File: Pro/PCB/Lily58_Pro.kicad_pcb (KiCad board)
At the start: 2 copper layers, 142.5 x 106.3 mm, 87 parts, among them J1 LED, J2 4PIN, J3 OLED, P1 i2c_pin, P2 i2c_pin, SW1 SW_PUSH, SW10 SW_PUSH, SW11 SW_PUSH, SW12 SW_PUSH, SW13 SW_PUSH, SW14 SW_PUSH, SW15 SW_PUSH, SW16 SW_PUSH, SW17 SW_PUSH, SW18 SW_PUSH, SW19 SW_PUSH, SW2 SW_PUSH, SW20 SW_PUSH, SW21 SW_PUSH, SW22 SW_PUSH, SW23 SW_PUSH, SW24 SW_PUSH, SW25 SW_PUSH, SW26 SW_PUSH, SW27 SW_PUSH, SW28 SW_PUSH, SW29 SW_PUSH, SW3 SW_PUSH, SW4 SW_PUSH, SW5 SW_PUSH, SW6 SW_PUSH, SW7 SW_PUSH, SW8 SW_PUSH, SW9 SW_PUSH, U1 ProMicro

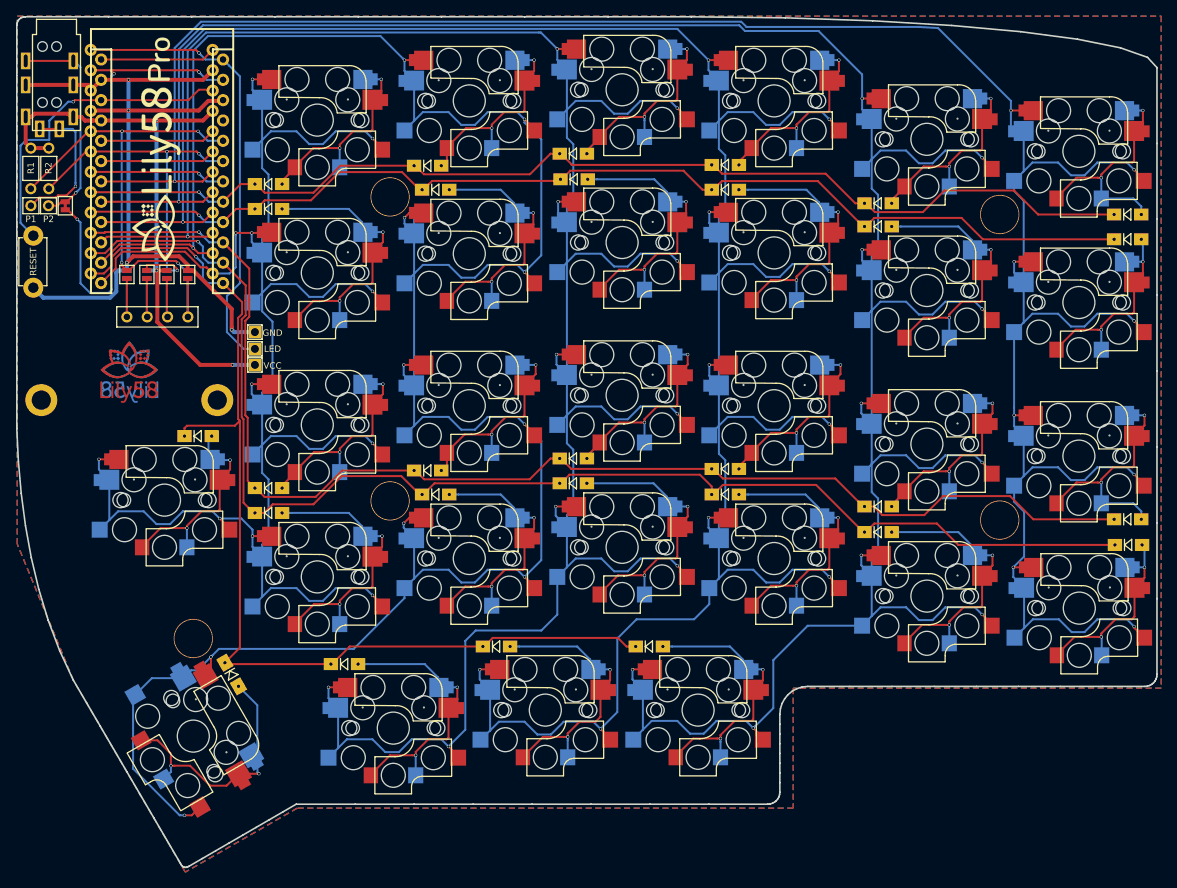
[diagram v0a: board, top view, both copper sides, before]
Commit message: Add footprints to Lily58 Pro library
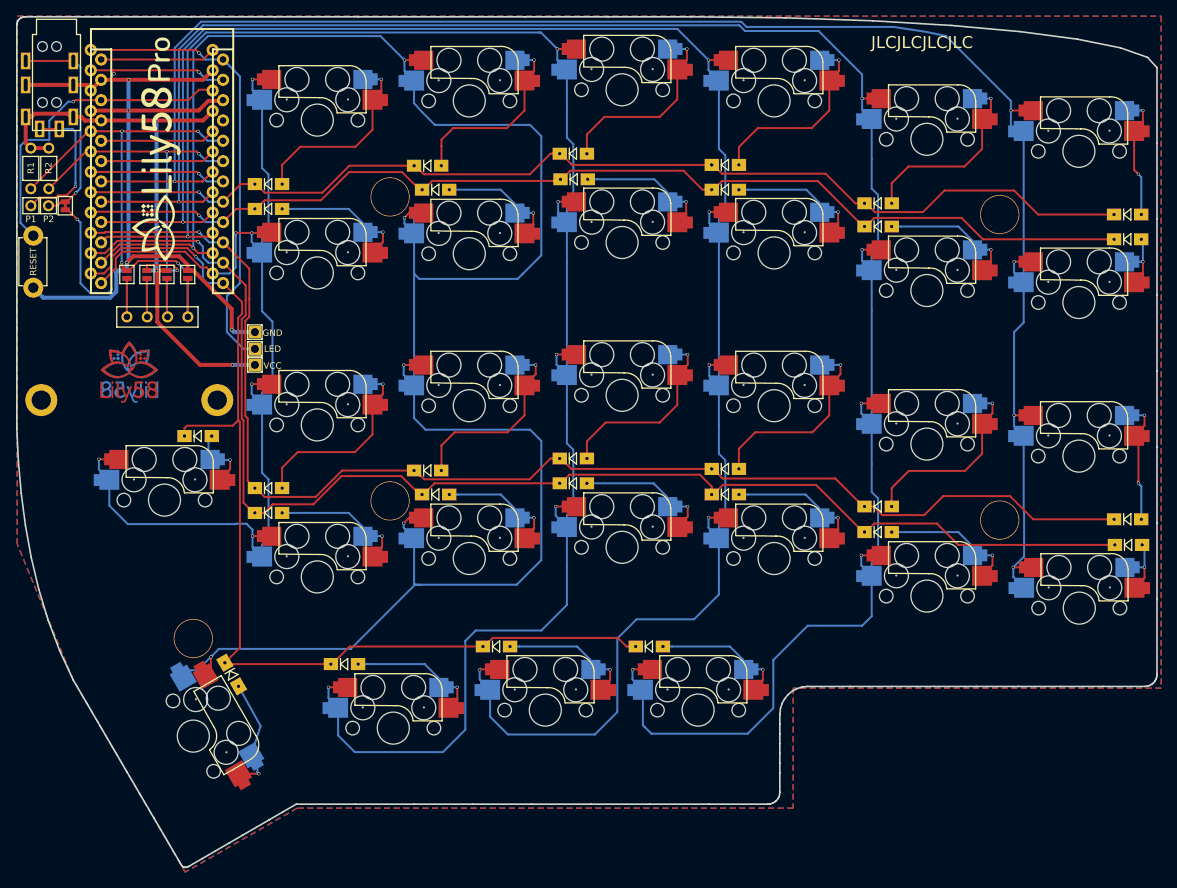
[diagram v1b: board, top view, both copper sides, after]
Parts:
- SW1, SW10, SW11, SW12, SW13, SW14, SW15, SW16, SW17, SW18, SW19, SW2, SW20, SW21, SW22, SW23, SW24, SW25, SW26, SW27, SW28, SW29, SW3, SW4, SW5, SW6, SW7, SW8, SW9: footprint Lily58-footprint:CherryMX_KailhLowProfile_Hotswap_edge -> Lily58_Pro-footprint:MX_Hotswap_dual_noled
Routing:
- net col5: track 235.9 -> 145.8 mm, vias 11 -> 6
- net col2: track 334.4 -> 251.7 mm, vias 11 -> 6
- net col3: track 319.9 -> 237.2 mm, vias 11 -> 6
- net col1: track 350.6 -> 268.6 mm, vias 11 -> 6
- net col0: track 304.4 -> 224.0 mm, vias 9 -> 5
- net col4: track 319.5 -> 270.4 mm, vias 11 -> 6
- net Net-(D26-Pad2): track 35.0 -> 16.5 mm, vias 2 -> 1
- net Net-(D19-Pad2): track 37.2 -> 19.1 mm, vias 2 -> 1
- net Net-(D12-Pad2): track 28.0 -> 9.92 mm, vias 2 -> 1
- net Net-(D27-Pad2): track 37.1 -> 19.0 mm, vias 2 -> 1
- net Net-(D9-Pad2): track 36.9 -> 18.8 mm, vias 2 -> 1
- net Net-(D22-Pad2): track 37.1 -> 19.0 mm, vias 2 -> 1
- net Net-(D11-Pad2): track 37.1 -> 19.0 mm, vias 2 -> 1
- net Net-(D10-Pad2): track 37.0 -> 18.9 mm, vias 2 -> 1
- net Net-(D28-Pad2): track 37.1 -> 19.1 mm, vias 2 -> 1
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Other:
- outline, holes or cut-outs redrawn
- rule via_min_size: 0.4 -> 0.3
- board text added: "JLCJLCJLCJLC"
